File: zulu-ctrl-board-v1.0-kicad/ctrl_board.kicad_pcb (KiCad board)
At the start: 2 copper layers, 79.6 x 45.2 mm, 34 parts, among them J1 Zulu I2C w/ interrupt Connect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, J2 OLED Connector, J5 CENTER_INT, J6 I2C Qwiic, J7 I2C Qwiic, J8 Zulu I2C w/ interrupt Connect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, SW1 SW_SPST, SW2 SW_SPST, SW4 Rotary_Encoder_Switch, U1 PCA9554APW,118

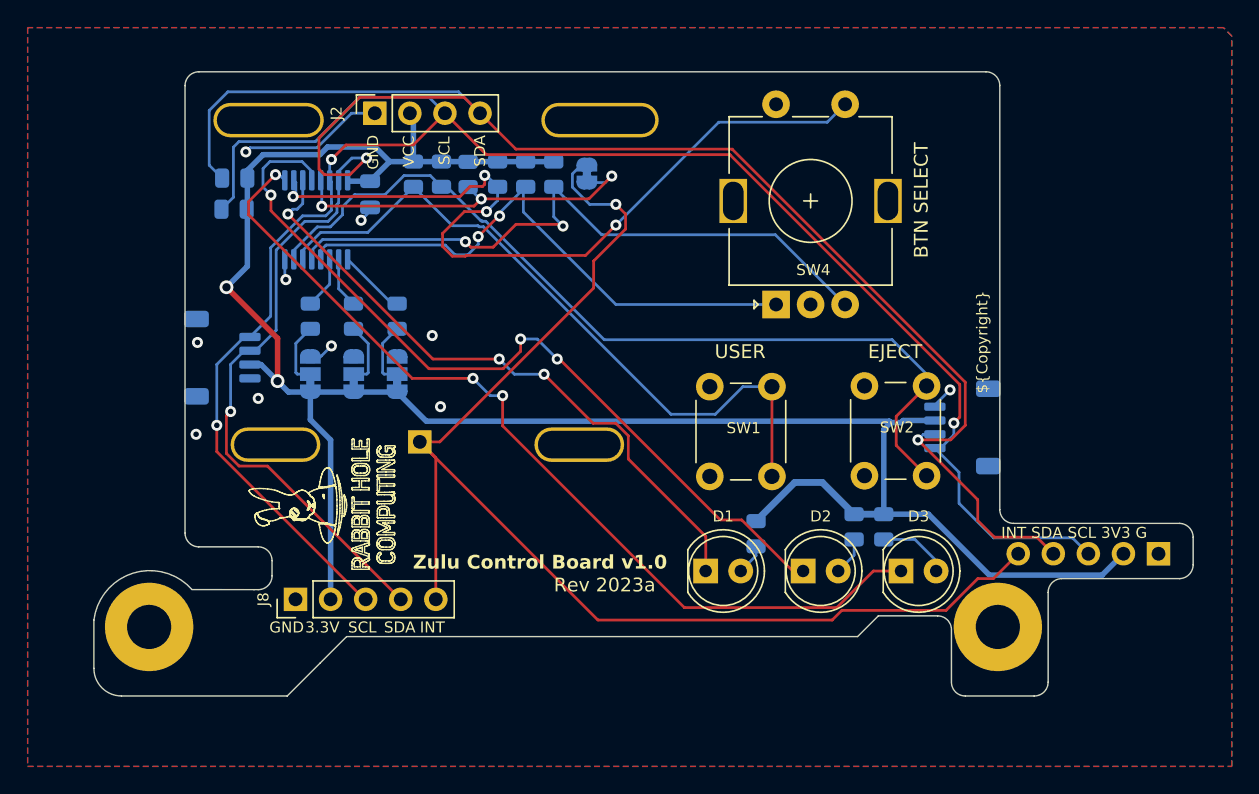
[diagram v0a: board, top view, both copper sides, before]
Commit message: Design of new rev
Dropped 2.54mm pitch I2C headers, except for display
Removed LEDs
Added two more mounting holes. Made all 4 of them 2.8mm holes
Decreased the size of the board
Moved buttons, rotary, and screen closer together
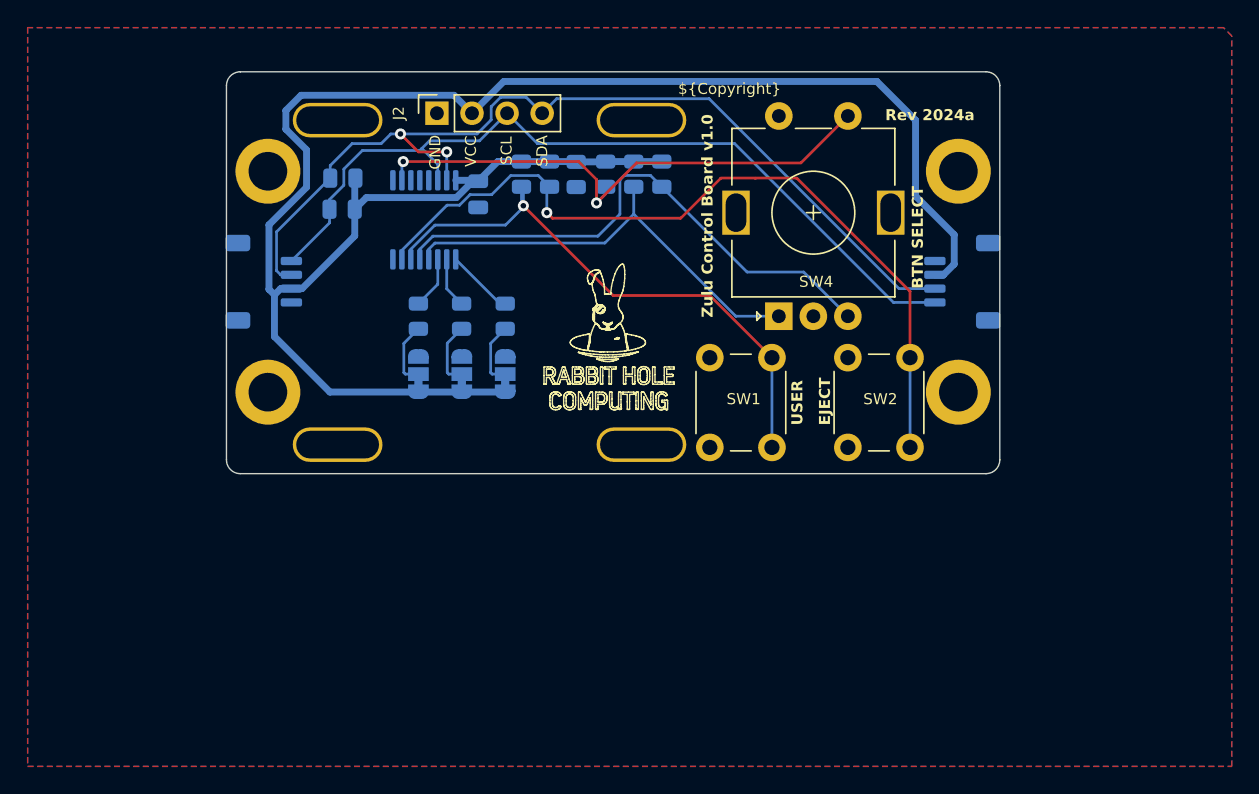
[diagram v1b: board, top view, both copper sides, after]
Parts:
- removed D1, D2, D3: LED, LED_THT:LED_D5.0mm
- removed J1, J8: Zulu I2C w/ interrupt Connector, Connector_PinHeader_2.54mm:PinHeader_1x05_P2.54mm_Vertical
- removed J5: CENTER_INT, Connector_PinHeader_2.54mm:PinHeader_1x01_P2.54mm_Vertical
- removed JP4: SolderJumper_2_Open, Jumper:SolderJumper-2_P1.3mm_Bridged_RoundedPad1.0x1.5mm
- removed R12, R13, R14: 10k, Resistor_SMD:R_0805_2012Metric
- added MK3: M2.5, rhc:MountingHole_2.8mm_M2.5custom_DIN965_Pad, F.Cu at (143.0, 162.0)
- added MK4: M2.5, rhc:MountingHole_2.8mm_M2.5custom_DIN965_Pad, F.Cu at (93.0, 162.0)
- MK1, MK2: value M3 -> M2.5; footprint MountingHole:MountingHole_3.2mm_M3_Pad -> rhc:MountingHole_2.8mm_M2.5custom_DIN965_Pad
- moved MK1 19.1 mm to (93.0, 178.0)
- moved MK2 17.2 mm to (143.0, 178.0)
- moved J6 10.6 mm to (143.3, 170.0)
- moved JP1 7.83 mm to (110.2, 176.7)
- moved JP2 7.83 mm to (107.0, 176.7)
- moved JP3 7.83 mm to (103.9, 176.7)
- moved R1 7.83 mm to (121.5, 162.2)
- moved R10 7.83 mm to (98.4, 164.8)
- moved R11 7.83 mm to (98.4, 162.5)
- moved R2 7.83 mm to (119.5, 162.2)
- moved R3 7.83 mm to (111.4, 162.2)
- moved R4 7.83 mm to (113.4, 162.2)
- moved R5 7.83 mm to (115.3, 162.2)
- moved R6 7.83 mm to (117.5, 162.2)
- moved R7 7.83 mm to (110.2, 172.5)
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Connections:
- R5 pad 1: Net-(JP4-A) -> unconnected-(R5-Pad1)
- U1 pad 11: /LED_1 -> unconnected-(U1-IO6-Pad11)
- U1 pad 12: /LED_2 -> unconnected-(U1-IO7-Pad12)
- U1 pad 13: Net-(JP4-A) -> unconnected-(R5-Pad1)
- U1 pad 9: /LED_3 -> unconnected-(U1-IO4-Pad9)
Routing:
- net /INT: track 93.0 -> 0.00 mm, vias 1 -> 0
- net /SDA: track 156.2 -> 69.4 mm, vias 3 -> 2
- net /SCL: track 139.5 -> 61.2 mm, vias 3 -> 0
- net /LED_3: track 66.0 -> 0.00 mm, vias 3 -> 0
- net /LED_2: track 59.6 -> 0.00 mm, vias 3 -> 0
- net /LED_1: track 46.5 -> 0.00 mm, vias 3 -> 0
- net Net-(JP4-A): track 27.1 -> 0.00 mm, vias 3 -> 0
- net /BUTTON_4: track 58.4 -> 39.9 mm, vias 4 -> 2
- net +3V3: track 153.1 -> 135.8 mm, vias 2 -> 0
- net GND: track 16.7 -> 0.00 mm, vias 10 -> 0
- net /ROTARY_ENC_A: track 41.4 -> 32.2 mm, vias 2 -> 0
- net /BUTTON_1: track 50.7 -> 42.1 mm, vias 0 -> 1
- net /ROTARY_ENC_B: track 47.9 -> 39.6 mm, vias 2 -> 0
- net /BUTTON_2: track 64.2 -> 58.2 mm, vias 0 -> 1
- net Net-(D3-A): track 5.18 -> 0.00 mm
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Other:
- board size 79.6 x 45.2 mm -> 56 x 29.1 mm
- board text added: "Derived from Tony Kuker's PiSCSI Control Board v1.6 project. Under BSD 3-Clause License"
- board text removed: "2 x M3"
- board text removed: "3.3V"
- board text removed: "Derived from Tony Kuker's PiSCSI Control Board v1.6 project. Under BSD 3-Clause License Copyright (c) 2020-2023 akuker"
- board text removed: "GND"
- board text removed: "INT"
- board text removed: "INT SDA SCL 3V3 G"
- board text removed: "SCL"
- board text removed: "SDA"

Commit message: Add dimensions and create step file
Added dimensions and adjusted some part locations to the nearest 0.1mm
Generated a 3D model step file
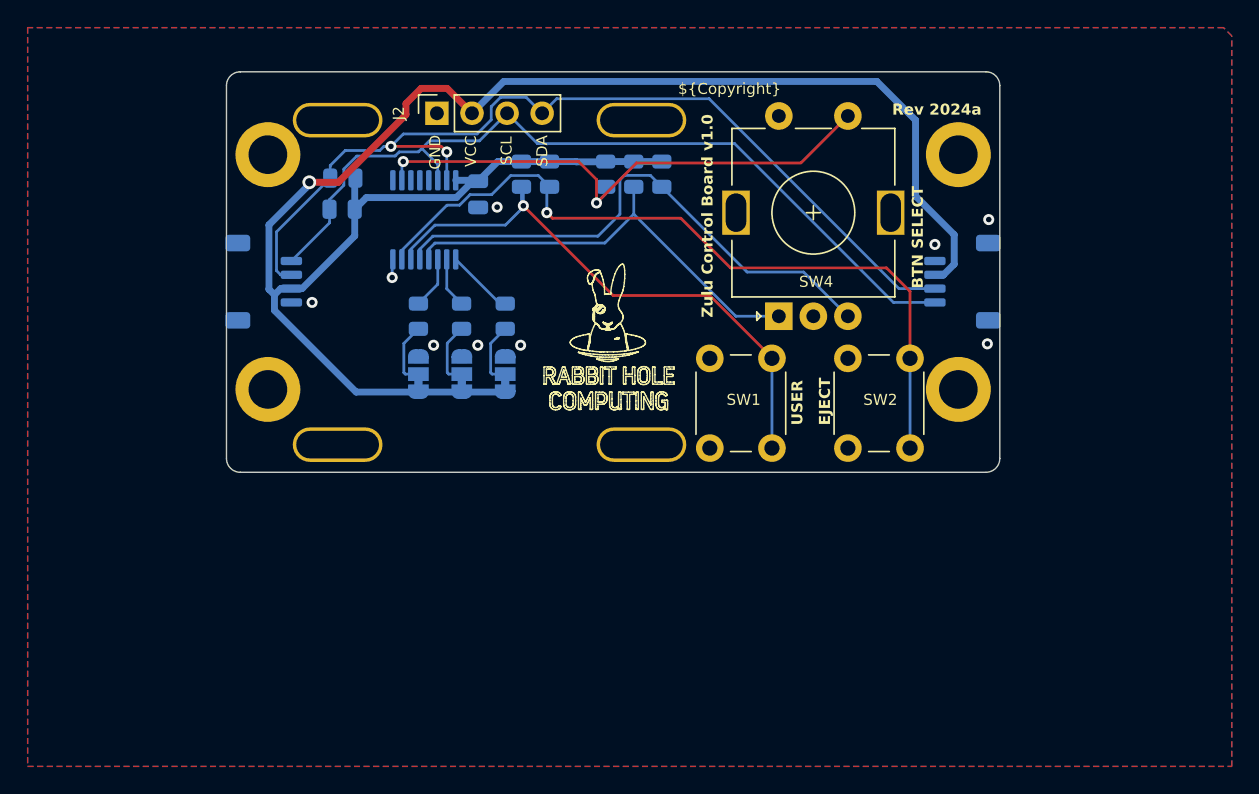
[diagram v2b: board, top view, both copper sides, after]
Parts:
- removed R5: 10k, Resistor_SMD:R_0805_2012Metric
- moved MK3 1.20 mm to (143.0, 160.8)
- moved MK4 1.20 mm to (93.0, 160.8)
- moved MK1 0.20 mm to (93.0, 177.8)
- moved MK2 0.20 mm to (143.0, 177.8)
- moved SW1 0.05 mm to (125.0, 182.1)
- moved SW2 0.05 mm to (135.0, 182.1)
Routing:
- net +3V3: track 135.8 -> 130.3 mm, vias 0 -> 1
- net /BUTTON_2: track 58.2 -> 55.9 mm
- net GND: track 0.00 -> 1.34 mm, vias 0 -> 9
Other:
- board size 56 x 29.1 mm -> 56 x 29 mm
